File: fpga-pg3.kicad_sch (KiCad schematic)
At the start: 1 part, among them U1 XC7A15T-FTG256

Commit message: stuff
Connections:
- net JTAG.TCK: now reaches U1.L7 (TCK_0)
- net JTAG.TMS: now reaches U1.M7 (TMS_0)
- net JTAG.TDI: now reaches U1.N7 (TDI_0)
- net JTAG.TDO: now reaches U1.N8 (TDO_0)
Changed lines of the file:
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@@
 	(generator_version "8.0")
 	(paper "A3")
+	(bus_entry
+		(at 273.05 129.54)
+		(size -2.54 2.54)
+		(stroke
+			(width 0)
+			(type default)
+		)
+	)
+	(bus_entry
+		(at 273.05 124.46)
+		(size -2.54 2.54)
+		(stroke
+			(width 0)
+			(type default)
+		)
+	)
+	(bus_entry
+		(at 273.05 127)
+		(size -2.54 2.54)
+		(stroke
+			(width 0)
+			(type default)
+		)
+	)
+	(bus_entry
+		(at 273.05 132.08)
+		(size -2.54 2.54)
+		(stroke
+			(width 0)
+			(type default)
+		)
+	)
+	(bus
+		(pts
+			(xy 273.05 129.54) (xy 273.05 127)
+		)
+		(stroke
+			(width 0)
+			(type default)
+		)
+	)
+	(bus
+		(pts
+			(xy 273.05 132.08) (xy 273.05 129.54)
+		)
+		(stroke
+			(width 0)
+			(type default)
+		)
+	)
+	(bus
+		(pts
+			(xy 273.05 127) (xy 273.05 124.46)
+		)
+		(stroke
+			(width 0)
+			(type default)
+		)
+	)
+	(bus
+		(pts
+			(xy 273.05 121.92) (xy 299.72 121.92)
+		)
+		(stroke
+			(width 0)
+			(type default)
+		)
+	)
+	(wire
+		(pts
+			(xy 252.73 134.62) (xy 270.51 134.62)
+		)
+		(stroke
+			(width 0)
+			(type default)
+		)
+	)
+	(wire
+		(pts
+			(xy 252.73 129.54) (xy 270.51 129.54)
+		)
+		(stroke
+			(width 0)
+			(type default)
+		)
+	)
+	(wire
+		(pts
+			(xy 252.73 132.08) (xy 270.51 132.08)
+		)
+		(stroke
+			(width 0)
+			(type default)
+		)
+	)
+	(bus
+		(pts
+			(xy 273.05 124.46) (xy 273.05 121.92)
+		)
+		(stroke
+			(width 0)
+			(type default)
+		)
+	)
+	(wire
+		(pts
+			(xy 252.73 127) (xy 270.51 127)
+		)
+		(stroke
+			(width 0)
+			(type default)
+		)
+	)
+	(label "JTAG{TDI TDO TMS TCK}"
+		(at 273.05 121.92 0)
+		(fields_autoplaced yes)
+		(effects
+			(font
+				(size 1.27 1.27)
+			)
+			(justify left bottom)
+		)
+	)
+	(label "JTAG.TCK"
+		(at 252.73 134.62 0)
+		(fields_autoplaced yes)
+		(effects
+			(font
+				(size 1.27 1.27)
+			)
+			(justify left bottom)
+		)
+	)
+	(label "JTAG.TMS"
+		(at 252.73 132.08 0)
+		(fields_autoplaced yes)
+		(effects
+			(font
+				(size 1.27 1.27)
+			)
+			(justify left bottom)
+		)
+	)
+	(label "JTAG.TDI"
+		(at 252.73 127 0)
+		(fields_autoplaced yes)
+		(effects
+			(font
+				(size 1.27 1.27)
+			)
+			(justify left bottom)
+		)
+	)
+	(label "JTAG.TDO"
+		(at 252.73 129.54 0)
+		(fields_autoplaced yes)
+		(effects
+			(font
+				(size 1.27 1.27)
+			)
+			(justify left bottom)
+		)
+	)
+	(hierarchical_label "JTAG"
+		(shape bidirectional)
+		(at 299.72 121.92 0)
+		(fields_autoplaced yes)
+		(effects
+			(font
+				(size 1.27 1.27)
+			)
+			(justify left)
+		)
+	)
 	(symbol
 		(lib_id "FPGA_Xilinx_Artix7:XC7A15T-FTG256")

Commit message: more stuff
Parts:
- added R16: 0, Resistor_SMD:R_0402_1005Metric_Pad0.72x0.64mm_HandSolder, symbol Device:R
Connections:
- net INT_FLASH_SPI_CLK: now reaches U1.E8 (CCLK_0)
- net INT_FLASH_SPI_CLK: now also R16.2
- new net FLASH_SPI.CLK: R16.1
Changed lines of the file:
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@@
+	(wire
+		(pts
+			(xy 283.21 139.7) (xy 252.73 139.7)
+		)
+		(stroke
+			(width 0)
+			(type default)
+		)
+	)
 	(wire
 		(pts
@@
 	(wire
 		(pts
-			(xy 252.73 129.54) (xy 270.51 129.54)
+			(xy 321.31 139.7) (xy 290.83 139.7)
 		)
 		(stroke
@@
 	(wire
 		(pts
-			(xy 252.73 132.08) (xy 270.51 132.08)
+			(xy 252.73 129.54) (xy 270.51 129.54)
 		)
 		(stroke
@@
 		)
 	)
+	(wire
+		(pts
+			(xy 252.73 132.08) (xy 270.51 132.08)
+		)
+		(stroke
+			(width 0)
+			(type default)
+		)
+	)
 	(bus
 		(pts
@@
 			(width 0)
 			(type default)
+		)
+	)
+	(label "FLASH_SPI.CLK"
+		(at 316.23 139.7 180)
+		(fields_autoplaced yes)
+		(effects
+			(font
+				(size 1.27 1.27)
+			)
+			(justify right bottom)
+		)
+	)
+	(label "INT_FLASH_SPI_CLK"
+		(at 278.13 139.7 180)
+		(fields_autoplaced yes)
+		(effects
+			(font
+				(size 1.27 1.27)
+			)
+			(justify right bottom)
 		)
 	)
@@
 				)
 			)
+		)
+	)
+	(symbol
+		(lib_id "Device:R")
+		(at 287.02 139.7 270)
+		(mirror x)
+		(unit 1)
+		(exclude_from_sim no)
+		(in_bom yes)
+		(on_board yes)
+		(dnp no)
+		(property "Reference" "R16"
+			(at 292.354 138.938 90)
+			(effects
+				(font
+					(size 1.27 1.27)
+				)
+			)
+		)
+		(property "Value" "0"
+			(at 282.448 138.684 90)
+			(effects
+				(font
+					(size 1.27 1.27)
+				)
+			)
+		)
+		(property "Footprint" "Resistor_SMD:R_0402_1005Metric_Pad0.72x0.64mm_HandSolder"
+			(at 287.02 141.478 90)
+			(effects
+				(font
+					(size 1.27 1.27)
+				)
+				(hide yes)
+			)
+		)
+		(property "Datasheet" "~"
+			(at 287.02 139.7 0)
+			(effects
+				(font
+					(size 1.27 1.27)
+				)
+				(hide yes)
+			)
+		)
+		(property "Description" ""
+			(at 287.02 139.7 0)
+			(effects
+				(font
+					(size 1.27 1.27)
+				)
+				(hide yes)
+			)
+		)
+		(property "LCSC" "C226391"
+			(at 287.02 139.7 0)
+			(effects
+				(font
+					(size 1.27 1.27)
+				)
+				(hide yes)
+			)
+		)
+		(pin "1"
+		)
+		(pin "2"
+		)
+		(instances
+			(project "logix-core"
+				(path "/cf3b7c5f-6ddc-4e3f-9529-0bcf5eec6f23/824409ff-e0aa-4944-ad80-228eadb659f9/9208eeea-aa23-4f0a-a0f4-52abaf751fbe"
+					(reference "R16")
+					(unit 1)
+				)
+			)

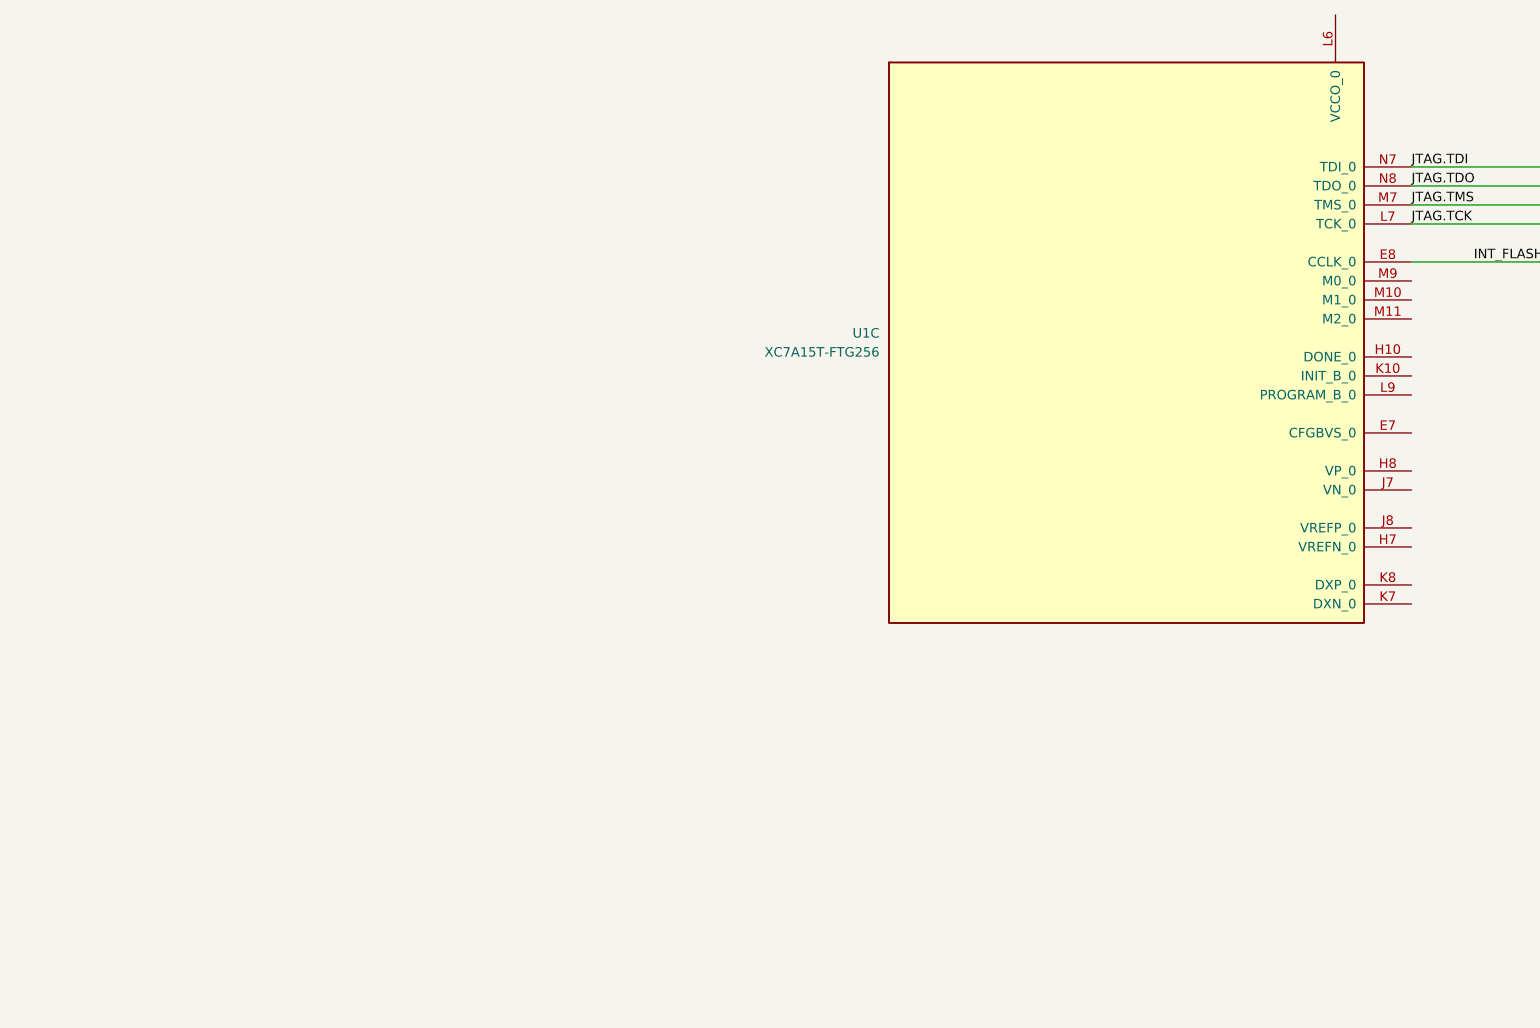
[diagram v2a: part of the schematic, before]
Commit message: changed ftg256 to csg325, wanted xc7a12t but couldnt find
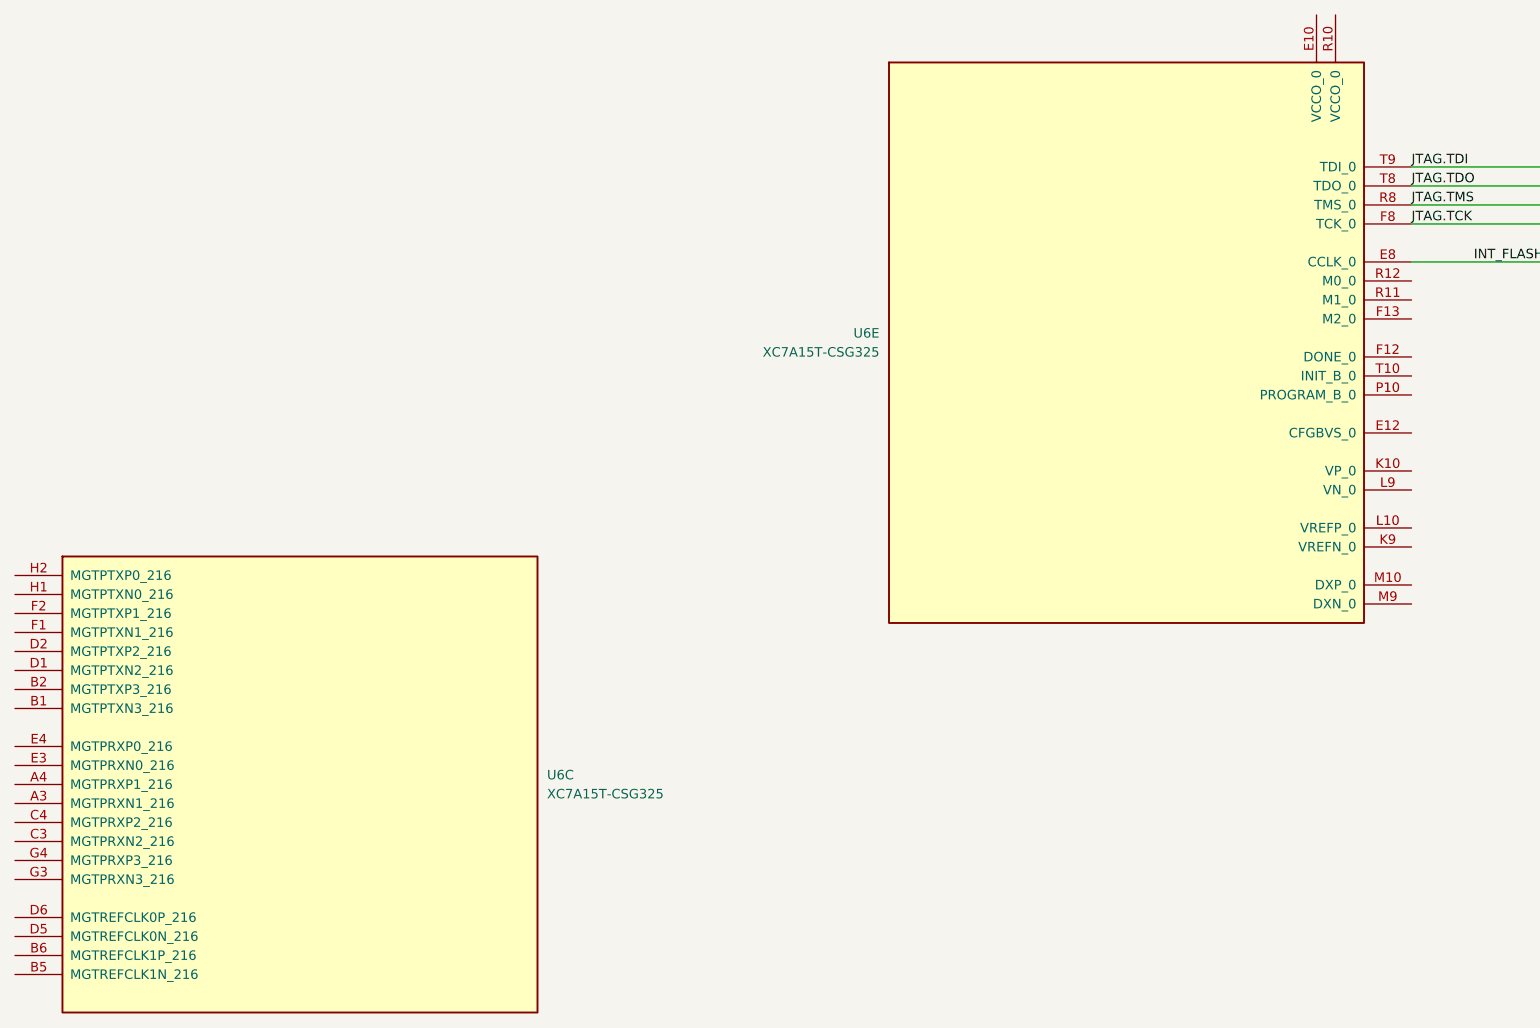
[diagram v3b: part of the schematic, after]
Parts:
- removed U1: XC7A15T-FTG256, Package_BGA:Xilinx_FTG256, symbol FPGA_Xilinx_Artix7:XC7A15T-FTG256
- added U6: XC7A15T-CSG325, Package_BGA:Xilinx_CSG325, symbol FPGA_Xilinx_Artix7:XC7A15T-CSG325
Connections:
- net INT_FLASH_SPI_CLK: now also U6.E8 (CCLK_0)
- net JTAG.TCK: now also U6.F8 (TCK_0)
- net JTAG.TDI: now also U6.T9 (TDI_0)
- net JTAG.TDO: now also U6.T8 (TDO_0)
- net JTAG.TMS: now also U6.R8 (TMS_0)

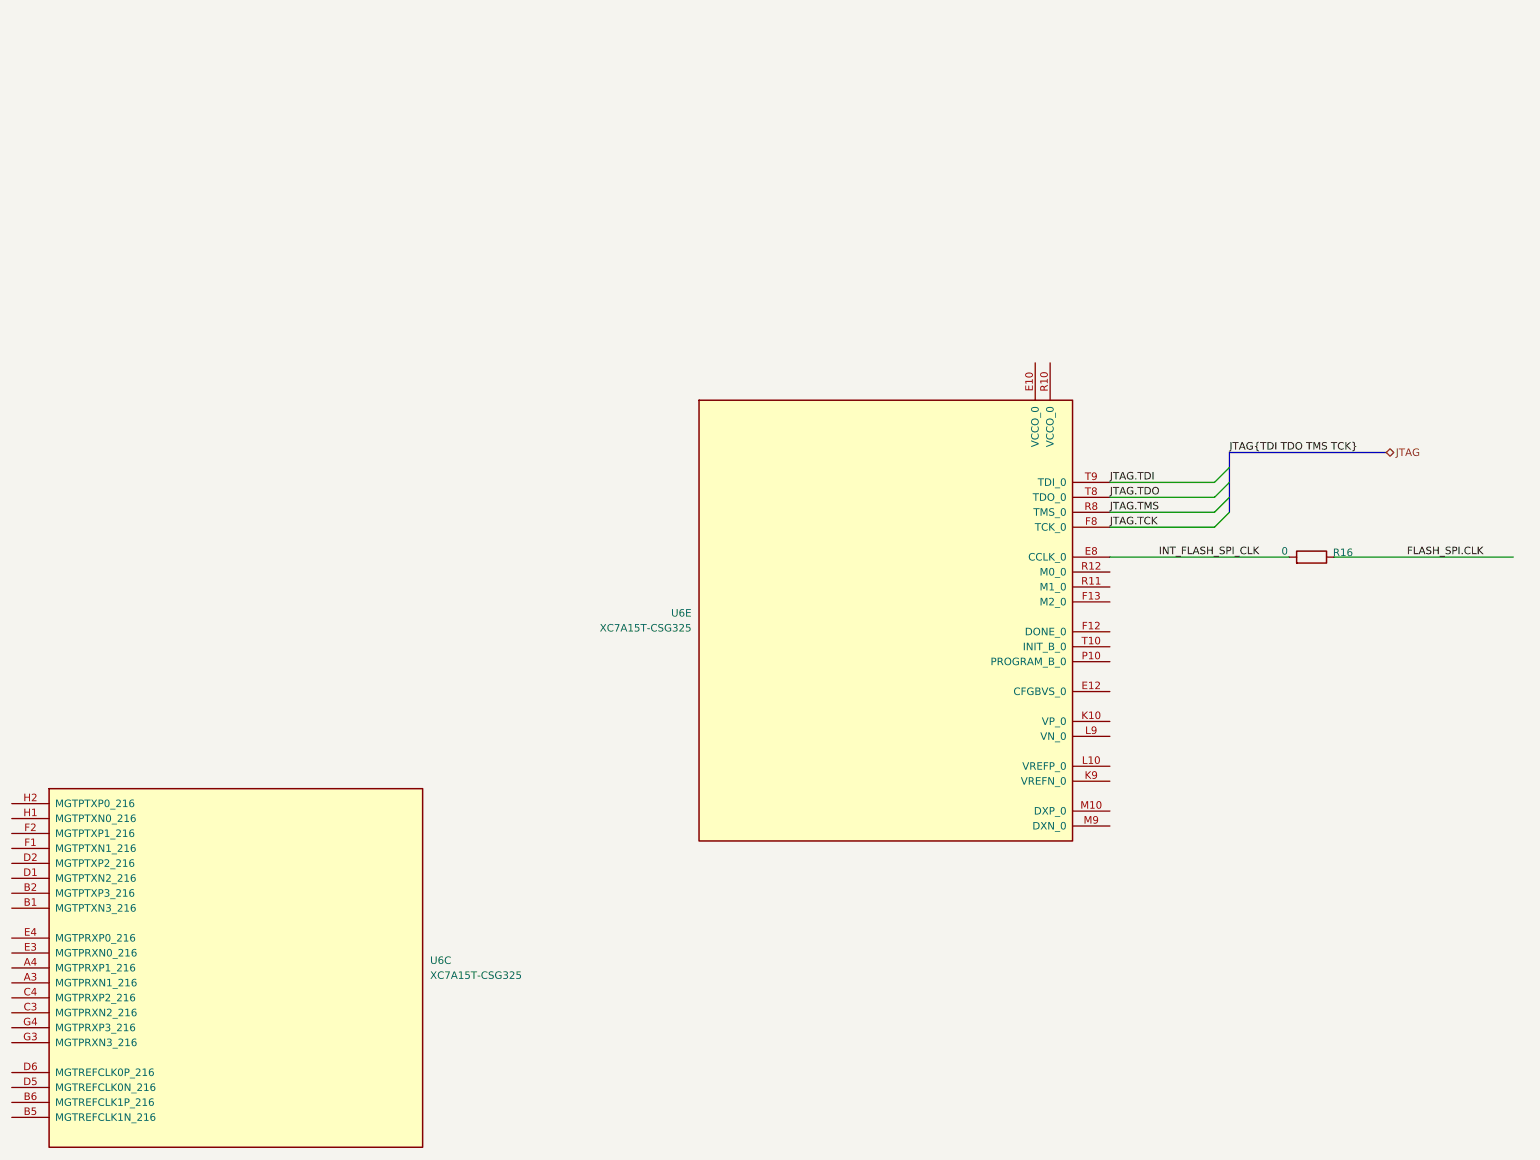
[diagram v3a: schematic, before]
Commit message: started mapping data input pins
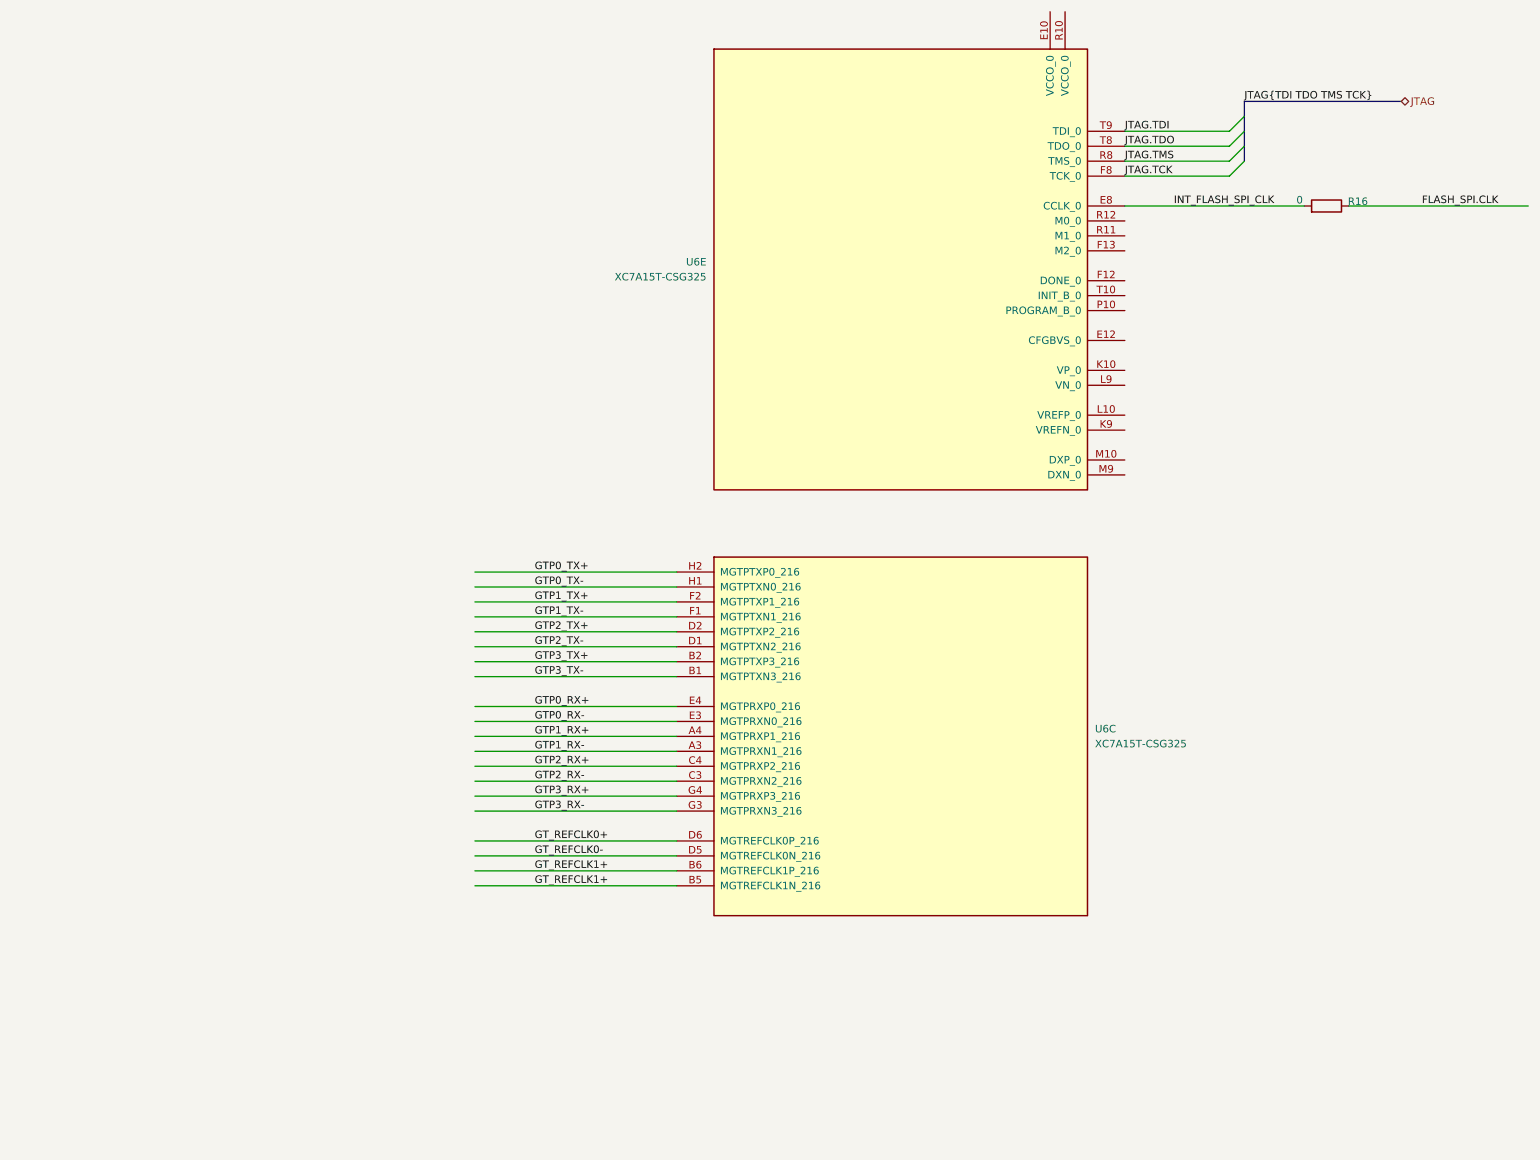
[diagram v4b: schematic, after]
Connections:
- net GTP1_RX-: now reaches U6.A3 (MGTPRXN1_216)
- net GTP1_RX+: now reaches U6.A4 (MGTPRXP1_216)
- net GTP3_TX-: now reaches U6.B1 (MGTPTXN3_216)
- net GTP3_TX+: now reaches U6.B2 (MGTPTXP3_216)
- net GT_REFCLK1+: now reaches U6.B5 (MGTREFCLK1N_216)
- net GT_REFCLK1+: now also U6.B6 (MGTREFCLK1P_216)
- net GTP2_RX-: now reaches U6.C3 (MGTPRXN2_216)
- net GTP2_RX+: now reaches U6.C4 (MGTPRXP2_216)
- net GTP2_TX-: now reaches U6.D1 (MGTPTXN2_216)
- net GTP2_TX+: now reaches U6.D2 (MGTPTXP2_216)
- net GT_REFCLK0-: now reaches U6.D5 (MGTREFCLK0N_216)
- net GT_REFCLK0+: now reaches U6.D6 (MGTREFCLK0P_216)
- net GTP0_RX-: now reaches U6.E3 (MGTPRXN0_216)
- net GTP0_RX+: now reaches U6.E4 (MGTPRXP0_216)
- net GTP1_TX-: now reaches U6.F1 (MGTPTXN1_216)
- net GTP1_TX+: now reaches U6.F2 (MGTPTXP1_216)
- net GTP3_RX-: now reaches U6.G3 (MGTPRXN3_216)
- net GTP3_RX+: now reaches U6.G4 (MGTPRXP3_216)
- net GTP0_TX-: now reaches U6.H1 (MGTPTXN0_216)
- net GTP0_TX+: now reaches U6.H2 (MGTPTXP0_216)
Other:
- moved on the sheet: R16, U6C, U6E
